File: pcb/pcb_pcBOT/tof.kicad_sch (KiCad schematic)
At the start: 3 parts, among them U1 VL53L0CXV0DH1

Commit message: Mise à jour du schéma TOF
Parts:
- added R1, R2: R, symbol Device:R
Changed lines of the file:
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@@
+	)
+	(symbol
+		(lib_id "Device:R")
+		(at 92.71 74.93 0)
+		(unit 1)
+		(exclude_from_sim no)
+		(in_bom yes)
+		(on_board yes)
+		(dnp no)
+		(fields_autoplaced yes)
+		(property "Reference" "R1"
+			(at 95.25 73.6599 0)
+			(effects
+				(font
+					(size 1.27 1.27)
+				)
+				(justify left)
+			)
+		)
+		(property "Value" "R"
+			(at 95.25 76.1999 0)
+			(effects
+				(font
+					(size 1.27 1.27)
+				)
+				(justify left)
+			)
+		)
+		(property "Footprint" ""
+			(at 90.932 74.93 90)
+			(effects
+				(font
+					(size 1.27 1.27)
+				)
+				(hide yes)
+			)
+		)
+		(property "Datasheet" "~"
+			(at 92.71 74.93 0)
+			(effects
+				(font
+					(size 1.27 1.27)
+				)
+				(hide yes)
+			)
+		)
+		(property "Description" "Resistor"
+			(at 92.71 74.93 0)
+			(effects
+				(font
+					(size 1.27 1.27)
+				)
+				(hide yes)
+			)
+		)
+		(pin "2"
+		)
+		(pin "1"
+		)
+		(instances
+			(project ""
+				(path "/bc28f26c-4b16-471a-8050-4a20f9c6df4f"
+					(reference "R1")
+					(unit 1)
+				)
+			)
+		)
 	)
 	(symbol
@@
 					(unit 1)
 				)
+			)
+		)
+	)
+	(symbol
+		(lib_id "Device:R")
+		(at 99.06 74.93 0)
+		(unit 1)
+		(exclude_from_sim no)
+		(in_bom yes)
+		(on_board yes)
+		(dnp no)
+		(fields_autoplaced yes)
+		(property "Reference" "R2"
+			(at 101.6 73.6599 0)
+			(effects
+				(font
+					(size 1.27 1.27)
+				)
+				(justify left)
+			)
+		)
+		(property "Value" "R"
+			(at 101.6 76.1999 0)
+			(effects
+				(font
+					(size 1.27 1.27)
+				)
+				(justify left)
+			)
+		)
+		(property "Footprint" ""
+			(at 97.282 74.93 90)
+			(effects
+				(font
+					(size 1.27 1.27)
+				)
+				(hide yes)
+			)
+		)
+		(property "Datasheet" "~"
+			(at 99.06 74.93 0)
+			(effects
+				(font
+					(size 1.27 1.27)
+				)
+				(hide yes)
+			)
+		)
+		(property "Description" "Resistor"
+			(at 99.06 74.93 0)
+			(effects
+				(font
+					(size 1.27 1.27)
+				)
+				(hide yes)
+			)
+		)
+		(pin "2"
+		)
+		(pin "1"
+		)
+		(instances
+			(project "tof"
+				(path "/bc28f26c-4b16-471a-8050-4a20f9c6df4f"
+					(reference "R2")
+					(unit 1)
+				)

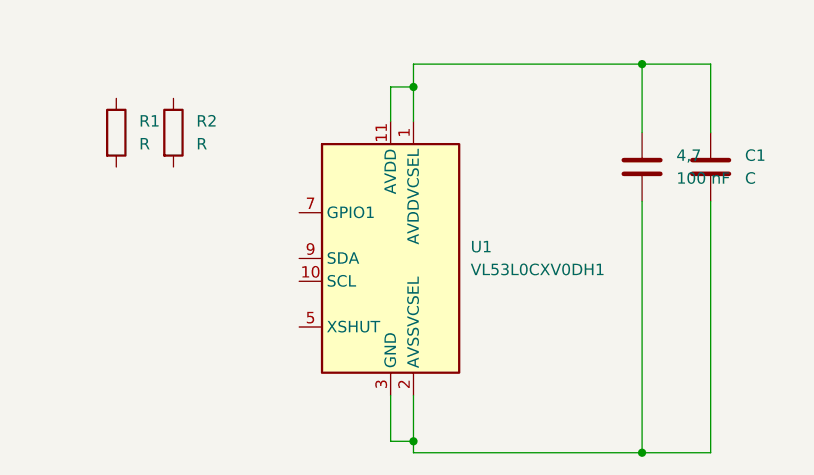
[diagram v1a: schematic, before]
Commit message: complement tof et connections, mise a jour du firmware
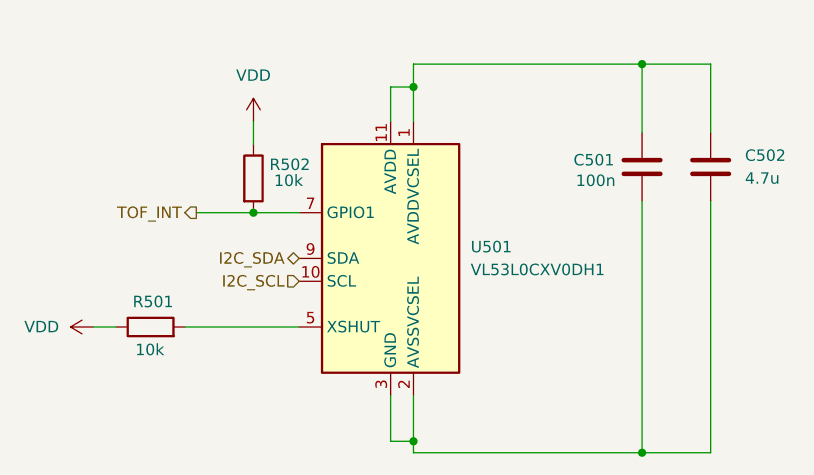
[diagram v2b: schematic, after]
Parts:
- removed 4,7: 100 nF, symbol Device:C
- removed C1: C, symbol Device:C
- removed R1, R2: R, symbol Device:R
- added C501: 100n, symbol Device:C
- added C502: 4.7u, symbol Device:C
- added R501, R502: 10k, symbol Device:R
- renumbered U1 to U501
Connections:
- net at U501.1 (AVDDVCSEL), U501.11 (AVDD): now also C501.1, C502.1
- net at U501.12 (GND), U501.2 (AVSSVCSEL), U501.3 (GND)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: now also C501.2, C502.2
- net I2C_SCL: now reaches U501.10 (SCL)
- net at U501.5 (XSHUT): now also R501.2
- net TOF_INT: now reaches U501.7 (GPIO1)
- net TOF_INT: now also R502.2
- net I2C_SDA: now reaches U501.9 (SDA)
- new net VDD: R501.1, R502.1
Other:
- company: (none) -> ENSEA G5
- title: (none) -> tof captor

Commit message: corrections d'erreurs et liasons bus i2c et spi
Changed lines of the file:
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@@
+	)
+	(symbol
+		(lib_id "power:VDD")
+		(at 163.83 68.58 0)
+		(unit 1)
+		(exclude_from_sim no)
+		(in_bom yes)
+		(on_board yes)
+		(dnp no)
+		(fields_autoplaced yes)
+		(property "Reference" "#PWR0503"
+			(at 163.83 72.39 0)
+			(effects
+				(font
+					(size 1.27 1.27)
+				)
+				(hide yes)
+			)
+		)
+		(property "Value" "VDD"
+			(at 163.83 63.5 0)
+			(effects
+				(font
+					(size 1.27 1.27)
+				)
+			)
+		)
+		(property "Footprint" ""
+			(at 163.83 68.58 0)
+			(effects
+				(font
+					(size 1.27 1.27)
+				)
+				(hide yes)
+			)
+		)
+		(property "Datasheet" ""
+			(at 163.83 68.58 0)
+			(effects
+				(font
+					(size 1.27 1.27)
+				)
+				(hide yes)
+			)
+		)
+		(property "Description" "Power symbol creates a global label with name \"VDD\""
+			(at 163.83 68.58 0)
+			(effects
+				(font
+					(size 1.27 1.27)
+				)
+				(hide yes)
+			)
+		)
+		(pin "1"
+		)
+		(instances
+			(project ""
+				(path "/704e4da3-8ee7-458f-8a0f-3fc97e8dc2a6/4d72a9a9-d017-47b1-aef2-c48a46b4c1d1"
+					(reference "#PWR0503")
+					(unit 1)
+				)
+			)
+		)
 	)
 	(symbol
